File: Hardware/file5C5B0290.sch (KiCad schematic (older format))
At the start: 24 parts, among them J14 Eurorack Connector, U10 LM1117-5.0, U11 L7809, U9 LM1117-3.3

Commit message: Started board layout
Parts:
- added C46, C47: 22 uF, Capacitors_SMD:CP_Elec_4x5.3, symbol Device:CP
- added C48: 100 nF, Capacitors_SMD:C_0603, symbol Device:C
- added FB4: Ferrite_Bead, symbol Device:Ferrite_Bead
- added U13: LM1117-3.3, TO_SOT_Packages_SMD:SOT-223-3_TabPin2, symbol Regulator_Linear:LM1117-3.3
- C33, C34, C35, C36, C37, C38, C42, C43: footprint (none) -> Capacitors_SMD:CP_Elec_4x5.3
- C39, C40, C41, C44: footprint (none) -> Capacitors_SMD:C_0603
- U10, U9: footprint (none) -> TO_SOT_Packages_SMD:SOT-223-3_TabPin2
- U11: footprint (none) -> TO_SOT_Packages_SMD:TO-252-3_TabPin2
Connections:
- net +12V: now also FB4.2
- net +3V3: now also C47.1, C48.1, U13.2 (VO); no longer C36.1, C39.1, U9.2 (VO)
- net GND: now also C46.2, C47.2, C48.2, U13.1 (GND)
- new net: C46.1, FB4.1, U13.3 (VI)
- new net +3.3VA: C36.1, C39.1, U9.2 (VO)
- no-connect marks 0 -> 6
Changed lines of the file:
@@
 F 0 "U9" H 3450 2992 50  0000 C CNN
 F 1 "LM1117-3.3" H 3450 2901 50  0000 C CNN
-F 2 "" H 3450 2750 50  0001 C CNN
+F 2 "TO_SOT_Packages_SMD:SOT-223-3_TabPin2" H 3450 2750 50  0001 C CNN
 F 3 "http://www.ti.com/lit/ds/symlink/lm1117.pdf" H 3450 2750 50  0001 C CNN
 	1    3450 2750
@@
 L power:+12V #PWR0204
 U 1 1 5C5B0D76
-P 2500 2500
-F 0 "#PWR0204" H 2500 2350 50  0001 C CNN
-F 1 "+12V" H 2515 2673 50  0000 C CNN
-F 2 "" H 2500 2500 50  0001 C CNN
-F 3 "" H 2500 2500 50  0001 C CNN
-	1    2500 2500
+P 2500 1400
+F 0 "#PWR0204" H 2500 1250 50  0001 C CNN
+F 1 "+12V" H 2515 1573 50  0000 C CNN
+F 2 "" H 2500 1400 50  0001 C CNN
+F 3 "" H 2500 1400 50  0001 C CNN
+	1    2500 1400
 	1    0    0    -1
 $EndComp
@@
 F 0 "C39" H 4565 2996 50  0000 L CNN
 F 1 "100 nF" H 4565 2905 50  0000 L CNN
-F 2 "" H 4488 2800 50  0001 C CNN
+F 2 "Capacitors_SMD:C_0603" H 4488 2800 50  0001 C CNN
 F 3 "~" H 4450 2950 50  0001 C CNN
 	1    4450 2950
@@
 L power:+3.3V #PWR0206
 U 1 1 5C5B1292
-P 4450 2500
-F 0 "#PWR0206" H 4450 2350 50  0001 C CNN
-F 1 "+3.3V" H 4465 2673 50  0000 C CNN
-F 2 "" H 4450 2500 50  0001 C CNN
-F 3 "" H 4450 2500 50  0001 C CNN
-	1    4450 2500
-	1    0    0    -1
-$EndComp
-Wire Wire Line
-	4450 2500 4450 2750
-Connection ~ 4450 2750
+P 4450 1400
+F 0 "#PWR0206" H 4450 1250 50  0001 C CNN
+F 1 "+3.3V" H 4465 1573 50  0000 C CNN
+F 2 "" H 4450 1400 50  0001 C CNN
+F 3 "" H 4450 1400 50  0001 C CNN
+	1    4450 1400
+	1    0    0    -1
+$EndComp
 $Comp
 L Connector_Generic:Conn_02x08_Odd_Even J14
@@
 F 0 "C33" H 2968 2996 50  0000 L CNN
 F 1 "22 uF" H 2968 2905 50  0000 L CNN
-F 2 "" H 2888 2800 50  0001 C CNN
+F 2 "Capacitors_SMD:CP_Elec_4x5.3" H 2888 2800 50  0001 C CNN
 F 3 "~" H 2850 2950 50  0001 C CNN
 	1    2850 2950
@@
 F 0 "C36" H 4068 2996 50  0000 L CNN
 F 1 "22 uF" H 4068 2905 50  0000 L CNN
-F 2 "" H 3988 2800 50  0001 C CNN
+F 2 "Capacitors_SMD:CP_Elec_4x5.3" H 3988 2800 50  0001 C CNN
 F 3 "~" H 3950 2950 50  0001 C CNN
 	1    3950 2950
@@
 F 0 "C42" H 7668 3546 50  0000 L CNN
 F 1 "22 uF" H 7668 3455 50  0000 L CNN
-F 2 "" H 7588 3350 50  0001 C CNN
+F 2 "Capacitors_SMD:CP_Elec_4x5.3" H 7588 3350 50  0001 C CNN
 F 3 "~" H 7550 3500 50  0001 C CNN
 	1    7550 3500
@@
 F 0 "C43" H 7668 3996 50  0000 L CNN
 F 1 "22 uF" H 7668 3905 50  0000 L CNN
-F 2 "" H 7588 3800 50  0001 C CNN
+F 2 "Capacitors_SMD:CP_Elec_4x5.3" H 7588 3800 50  0001 C CNN
 F 3 "~" H 7550 3950 50  0001 C CNN
 	1    7550 3950
@@
 F 0 "C40" H 4565 3996 50  0000 L CNN
 F 1 "100 nF" H 4565 3905 50  0000 L CNN
-F 2 "" H 4488 3800 50  0001 C CNN
+F 2 "Capacitors_SMD:C_0603" H 4488 3800 50  0001 C CNN
 F 3 "~" H 4450 3950 50  0001 C CNN
 	1    4450 3950
@@
 F 0 "C34" H 2968 3996 50  0000 L CNN
 F 1 "22 uF" H 2968 3905 50  0000 L CNN
-F 2 "" H 2888 3800 50  0001 C CNN
+F 2 "Capacitors_SMD:CP_Elec_4x5.3" H 2888 3800 50  0001 C CNN
 F 3 "~" H 2850 3950 50  0001 C CNN
 	1    2850 3950
@@
 F 0 "C37" H 4068 3996 50  0000 L CNN
 F 1 "22 uF" H 4068 3905 50  0000 L CNN
-F 2 "" H 3988 3800 50  0001 C CNN
+F 2 "Capacitors_SMD:CP_Elec_4x5.3" H 3988 3800 50  0001 C CNN
 F 3 "~" H 3950 3950 50  0001 C CNN
 	1    3950 3950
@@
 F 0 "U10" H 3450 3992 50  0000 C CNN
 F 1 "LM1117-5.0" H 3450 3901 50  0000 C CNN
-F 2 "" H 3450 3750 50  0001 C CNN
+F 2 "TO_SOT_Packages_SMD:SOT-223-3_TabPin2" H 3450 3750 50  0001 C CNN
 F 3 "http://www.ti.com/lit/ds/symlink/lm1117.pdf" H 3450 3750 50  0001 C CNN
 	1    3450 3750
@@
 F 0 "C41" H 4565 4996 50  0000 L CNN
 F 1 "100 nF" H 4565 4905 50  0000 L CNN
-F 2 "" H 4488 4800 50  0001 C CNN
+F 2 "Capacitors_SMD:C_0603" H 4488 4800 50  0001 C CNN
 F 3 "~" H 4450 4950 50  0001 C CNN
 	1    4450 4950
@@
 F 0 "C35" H 2968 4996 50  0000 L CNN
 F 1 "22 uF" H 2968 4905 50  0000 L CNN
-F 2 "" H 2888 4800 50  0001 C CNN
+F 2 "Capacitors_SMD:CP_Elec_4x5.3" H 2888 4800 50  0001 C CNN
 F 3 "~" H 2850 4950 50  0001 C CNN
 	1    2850 4950
@@
 F 0 "C38" H 4068 4996 50  0000 L CNN
 F 1 "22 uF" H 4068 4905 50  0000 L CNN
-F 2 "" H 3988 4800 50  0001 C CNN
+F 2 "Capacitors_SMD:CP_Elec_4x5.3" H 3988 4800 50  0001 C CNN
 F 3 "~" H 3950 4950 50  0001 C CNN
 	1    3950 4950
@@
 F 0 "U11" H 3450 4992 50  0000 C CNN
 F 1 "L7809" H 3450 4901 50  0000 C CNN
-F 2 "" H 3475 4600 50  0001 L CIN
+F 2 "TO_SOT_Packages_SMD:TO-252-3_TabPin2" H 3475 4600 50  0001 L CIN
 F 3 "http://www.st.com/content/ccc/resource/technical/document/datasheet/41/4f/b3/b0/12/d4/47/88/CD00000444.pdf/files/CD00000444.pdf/jcr:content/translations/en.CD00000444.pdf" H 3450 4700 50  0001 C CNN
 	1    3450 4750
@@
 F 0 "C44" H 8965 3996 50  0000 L CNN
 F 1 "100 nF" H 8965 3905 50  0000 L CNN
-F 2 "" H 8888 3800 50  0001 C CNN
+F 2 "Capacitors_SMD:C_0603" H 8888 3800 50  0001 C CNN
 F 3 "~" H 8850 3950 50  0001 C CNN
 	1    8850 3950
@@
 	0    1    1    0
 $EndComp
-Wire Wire Line
-	2500 2500 2500 2750
 Connection ~ 2500 3750
 Wire Wire Line
@@
 	0    1    1    0
 $EndComp
+Wire Wire Line
+	2500 2750 2500 3750
+$Comp
+L Regulator_Linear:LM1117-3.3 U13
+U 1 1 5BDDA893
+P 3450 1750
+F 0 "U13" H 3450 1992 50  0000 C CNN
+F 1 "LM1117-3.3" H 3450 1901 50  0000 C CNN
+F 2 "TO_SOT_Packages_SMD:SOT-223-3_TabPin2" H 3450 1750 50  0001 C CNN
+F 3 "http://www.ti.com/lit/ds/symlink/lm1117.pdf" H 3450 1750 50  0001 C CNN
+	1    3450 1750
+	1    0    0    -1
+$EndComp
+Wire Wire Line
+	2850 1750 3150 1750
+$Comp
+L power:GND #PWR010
+U 1 1 5BDDA89B
+P 3450 2200
+F 0 "#PWR010" H 3450 1950 50  0001 C CNN
+F 1 "GND" H 3455 2027 50  0000 C CNN
+F 2 "" H 3450 2200 50  0001 C CNN
+F 3 "" H 3450 2200 50  0001 C CNN
+	1    3450 2200
+	1    0    0    -1
+$EndComp
+Wire Wire Line
+	3450 2200 3450 2150
+Wire Wire Line
+	2850 1800 2850 1750
+Wire Wire Line
+	2850 1750 2800 1750
+Connection ~ 2850 1750
+Wire Wire Line
+	2850 2100 2850 2150
+Wire Wire Line
+	2850 2150 3450 2150
+Connection ~ 3450 2150
+Wire Wire Line
+	3450 2150 3450 2050
+Wire Wire Line
+	3450 2150 3950 2150
+Wire Wire Line
+	3950 2150 3950 2100
+Wire Wire Line
+	3950 1800 3950 1750
+Wire Wire Line
+	3950 1750 3750 1750
+$Comp
+L Device:C C48
+U 1 1 5BDDA8AD
+P 4450 1950
+F 0 "C48" H 4565 1996 50  0000 L CNN
+F 1 "100 nF" H 4565 1905 50  0000 L CNN
+F 2 "Capacitors_SMD:C_0603" H 4488 1800 50  0001 C CNN
+F 3 "~" H 4450 1950 50  0001 C CNN
+	1    4450 1950
+	1    0    0    -1
+$EndComp
+Wire Wire Line
+	4450 2100 4450 2150
+Wire Wire Line
+	4450 2150 3950 2150
+Connection ~ 3950 2150
+Wire Wire Line
+	3950 1750 4450 1750
+Wire Wire Line
+	4450 1750 4450 1800
+Connection ~ 3950 1750
+$Comp
+L Device:CP C46
+U 1 1 5BDDA8BC
+P 2850 1950
+F 0 "C46" H 2968 1996 50  0000 L CNN
+F 1 "22 uF" H 2968 1905 50  0000 L CNN
+F 2 "Capacitors_SMD:CP_Elec_4x5.3" H 2888 1800 50  0001 C CNN
+F 3 "~" H 2850 1950 50  0001 C CNN
+	1    2850 1950
+	1    0    0    -1
+$EndComp
+$Comp
+L Device:CP C47
+U 1 1 5BDDA8C3
+P 3950 1950
+F 0 "C47" H 4068 1996 50  0000 L CNN
+F 1 "22 uF" H 4068 1905 50  0000 L CNN
+F 2 "Capacitors_SMD:CP_Elec_4x5.3" H 3988 1800 50  0001 C CNN
+F 3 "~" H 3950 1950 50  0001 C CNN
+	1    3950 1950
+	1    0    0    -1
+$EndComp
+$Comp
+L Device:Ferrite_Bead FB4
+U 1 1 5BDDA8CB
+P 2650 1750
+F 0 "FB4" V 2376 1750 50  0000 C CNN
+F 1 "Ferrite_Bead" V 2467 1750 50  0000 C CNN
+F 2 "" V 2580 1750 50  0001 C CNN
+F 3 "~" H 2650 1750 50  0001 C CNN
+	1    2650 1750
+	0    1    1    0
+$EndComp
+Connection ~ 2500 1750
+Connection ~ 4450 1750
+$Comp
+L power:+3.3VA #PWR011
+U 1 1 5BDE9E2A
+P 4450 2650
+F 0 "#PWR011" H 4450 2500 50  0001 C CNN
+F 1 "+3.3VA" H 4465 2823 50  0000 C CNN
+F 2 "" H 4450 2650 50  0001 C CNN
+F 3 "" H 4450 2650 50  0001 C CNN
+	1    4450 2650
+	1    0    0    -1
+$EndComp
+Wire Wire Line
+	4450 2650 4450 2750
+Connection ~ 4450 2750
+Wire Wire Line
+	2500 1400 2500 1750
+Wire Wire Line
+	4450 1400 4450 1750
+Wire Wire Line
+	2500 1750 2500 2750
 Connection ~ 2500 2750
-Wire Wire Line
-	2500 2750 2500 3750
+NoConn ~ 5750 3350
+NoConn ~ 5750 3450
+NoConn ~ 5750 3550
+NoConn ~ 6250 3350
+NoConn ~ 6250 3450
+NoConn ~ 6250 3550
 $EndSCHEMATC

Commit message: Fixed issues with footprints
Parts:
- C33, C34, C35, C36, C37, C38, C42, C43, C46, C47: footprint Capacitors_SMD:CP_Elec_4x5.3 -> Capacitor_SMD:CP_Elec_4x5.3
- C39, C40, C41, C44, C48: footprint Capacitors_SMD:C_0603 -> Capacitor_SMD:C_0603_1608Metric
- U10, U13, U9: footprint TO_SOT_Packages_SMD:SOT-223-3_TabPin2 -> Package_TO_SOT_SMD:SOT-223-3_TabPin2
- U11: footprint TO_SOT_Packages_SMD:TO-252-3_TabPin2 -> Package_TO_SOT_SMD:TO-252-3_TabPin2
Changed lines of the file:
@@
 F 0 "U9" H 3450 2992 50  0000 C CNN
 F 1 "LM1117-3.3" H 3450 2901 50  0000 C CNN
-F 2 "TO_SOT_Packages_SMD:SOT-223-3_TabPin2" H 3450 2750 50  0001 C CNN
+F 2 "Package_TO_SOT_SMD:SOT-223-3_TabPin2" H 3450 2750 50  0001 C CNN
 F 3 "http://www.ti.com/lit/ds/symlink/lm1117.pdf" H 3450 2750 50  0001 C CNN
 	1    3450 2750
@@
 F 0 "C39" H 4565 2996 50  0000 L CNN
 F 1 "100 nF" H 4565 2905 50  0000 L CNN
-F 2 "Capacitors_SMD:C_0603" H 4488 2800 50  0001 C CNN
+F 2 "Capacitor_SMD:C_0603_1608Metric" H 4488 2800 50  0001 C CNN
 F 3 "~" H 4450 2950 50  0001 C CNN
 	1    4450 2950
@@
 F 0 "C33" H 2968 2996 50  0000 L CNN
 F 1 "22 uF" H 2968 2905 50  0000 L CNN
-F 2 "Capacitors_SMD:CP_Elec_4x5.3" H 2888 2800 50  0001 C CNN
+F 2 "Capacitor_SMD:CP_Elec_4x5.3" H 2888 2800 50  0001 C CNN
 F 3 "~" H 2850 2950 50  0001 C CNN
 	1    2850 2950
@@
 F 0 "C36" H 4068 2996 50  0000 L CNN
 F 1 "22 uF" H 4068 2905 50  0000 L CNN
-F 2 "Capacitors_SMD:CP_Elec_4x5.3" H 3988 2800 50  0001 C CNN
+F 2 "Capacitor_SMD:CP_Elec_4x5.3" H 3988 2800 50  0001 C CNN
 F 3 "~" H 3950 2950 50  0001 C CNN
 	1    3950 2950
@@
 F 0 "C42" H 7668 3546 50  0000 L CNN
 F 1 "22 uF" H 7668 3455 50  0000 L CNN
-F 2 "Capacitors_SMD:CP_Elec_4x5.3" H 7588 3350 50  0001 C CNN
+F 2 "Capacitor_SMD:CP_Elec_4x5.3" H 7588 3350 50  0001 C CNN
 F 3 "~" H 7550 3500 50  0001 C CNN
 	1    7550 3500
@@
 F 0 "C43" H 7668 3996 50  0000 L CNN
 F 1 "22 uF" H 7668 3905 50  0000 L CNN
-F 2 "Capacitors_SMD:CP_Elec_4x5.3" H 7588 3800 50  0001 C CNN
+F 2 "Capacitor_SMD:CP_Elec_4x5.3" H 7588 3800 50  0001 C CNN
 F 3 "~" H 7550 3950 50  0001 C CNN
 	1    7550 3950
@@
 F 0 "C40" H 4565 3996 50  0000 L CNN
 F 1 "100 nF" H 4565 3905 50  0000 L CNN
-F 2 "Capacitors_SMD:C_0603" H 4488 3800 50  0001 C CNN
+F 2 "Capacitor_SMD:C_0603_1608Metric" H 4488 3800 50  0001 C CNN
 F 3 "~" H 4450 3950 50  0001 C CNN
 	1    4450 3950
@@
 F 0 "C34" H 2968 3996 50  0000 L CNN
 F 1 "22 uF" H 2968 3905 50  0000 L CNN
-F 2 "Capacitors_SMD:CP_Elec_4x5.3" H 2888 3800 50  0001 C CNN
+F 2 "Capacitor_SMD:CP_Elec_4x5.3" H 2888 3800 50  0001 C CNN
 F 3 "~" H 2850 3950 50  0001 C CNN
 	1    2850 3950
@@
 F 0 "C37" H 4068 3996 50  0000 L CNN
 F 1 "22 uF" H 4068 3905 50  0000 L CNN
-F 2 "Capacitors_SMD:CP_Elec_4x5.3" H 3988 3800 50  0001 C CNN
+F 2 "Capacitor_SMD:CP_Elec_4x5.3" H 3988 3800 50  0001 C CNN
 F 3 "~" H 3950 3950 50  0001 C CNN
 	1    3950 3950
@@
 F 0 "U10" H 3450 3992 50  0000 C CNN
 F 1 "LM1117-5.0" H 3450 3901 50  0000 C CNN
-F 2 "TO_SOT_Packages_SMD:SOT-223-3_TabPin2" H 3450 3750 50  0001 C CNN
+F 2 "Package_TO_SOT_SMD:SOT-223-3_TabPin2" H 3450 3750 50  0001 C CNN
 F 3 "http://www.ti.com/lit/ds/symlink/lm1117.pdf" H 3450 3750 50  0001 C CNN
 	1    3450 3750
@@
 F 0 "C41" H 4565 4996 50  0000 L CNN
 F 1 "100 nF" H 4565 4905 50  0000 L CNN
-F 2 "Capacitors_SMD:C_0603" H 4488 4800 50  0001 C CNN
+F 2 "Capacitor_SMD:C_0603_1608Metric" H 4488 4800 50  0001 C CNN
 F 3 "~" H 4450 4950 50  0001 C CNN
 	1    4450 4950
@@
 F 0 "C35" H 2968 4996 50  0000 L CNN
 F 1 "22 uF" H 2968 4905 50  0000 L CNN
-F 2 "Capacitors_SMD:CP_Elec_4x5.3" H 2888 4800 50  0001 C CNN
+F 2 "Capacitor_SMD:CP_Elec_4x5.3" H 2888 4800 50  0001 C CNN
 F 3 "~" H 2850 4950 50  0001 C CNN
 	1    2850 4950
@@
 F 0 "C38" H 4068 4996 50  0000 L CNN
 F 1 "22 uF" H 4068 4905 50  0000 L CNN
-F 2 "Capacitors_SMD:CP_Elec_4x5.3" H 3988 4800 50  0001 C CNN
+F 2 "Capacitor_SMD:CP_Elec_4x5.3" H 3988 4800 50  0001 C CNN
 F 3 "~" H 3950 4950 50  0001 C CNN
 	1    3950 4950
@@
 F 0 "U11" H 3450 4992 50  0000 C CNN
 F 1 "L7809" H 3450 4901 50  0000 C CNN
-F 2 "TO_SOT_Packages_SMD:TO-252-3_TabPin2" H 3475 4600 50  0001 L CIN
+F 2 "Package_TO_SOT_SMD:TO-252-3_TabPin2" H 3475 4600 50  0001 L CIN
 F 3 "http://www.st.com/content/ccc/resource/technical/document/datasheet/41/4f/b3/b0/12/d4/47/88/CD00000444.pdf/files/CD00000444.pdf/jcr:content/translations/en.CD00000444.pdf" H 3450 4700 50  0001 C CNN
 	1    3450 4750
@@
 F 0 "C44" H 8965 3996 50  0000 L CNN
 F 1 "100 nF" H 8965 3905 50  0000 L CNN
-F 2 "Capacitors_SMD:C_0603" H 8888 3800 50  0001 C CNN
+F 2 "Capacitor_SMD:C_0603_1608Metric" H 8888 3800 50  0001 C CNN
 F 3 "~" H 8850 3950 50  0001 C CNN
 	1    8850 3950
@@
 F 0 "U13" H 3450 1992 50  0000 C CNN
 F 1 "LM1117-3.3" H 3450 1901 50  0000 C CNN
-F 2 "TO_SOT_Packages_SMD:SOT-223-3_TabPin2" H 3450 1750 50  0001 C CNN
+F 2 "Package_TO_SOT_SMD:SOT-223-3_TabPin2" H 3450 1750 50  0001 C CNN
 F 3 "http://www.ti.com/lit/ds/symlink/lm1117.pdf" H 3450 1750 50  0001 C CNN
 	1    3450 1750
@@
 F 0 "C48" H 4565 1996 50  0000 L CNN
 F 1 "100 nF" H 4565 1905 50  0000 L CNN
-F 2 "Capacitors_SMD:C_0603" H 4488 1800 50  0001 C CNN
+F 2 "Capacitor_SMD:C_0603_1608Metric" H 4488 1800 50  0001 C CNN
 F 3 "~" H 4450 1950 50  0001 C CNN
 	1    4450 1950
@@
 F 0 "C46" H 2968 1996 50  0000 L CNN
 F 1 "22 uF" H 2968 1905 50  0000 L CNN
-F 2 "Capacitors_SMD:CP_Elec_4x5.3" H 2888 1800 50  0001 C CNN
+F 2 "Capacitor_SMD:CP_Elec_4x5.3" H 2888 1800 50  0001 C CNN
 F 3 "~" H 2850 1950 50  0001 C CNN
 	1    2850 1950
@@
 F 0 "C47" H 4068 1996 50  0000 L CNN
 F 1 "22 uF" H 4068 1905 50  0000 L CNN
-F 2 "Capacitors_SMD:CP_Elec_4x5.3" H 3988 1800 50  0001 C CNN
+F 2 "Capacitor_SMD:CP_Elec_4x5.3" H 3988 1800 50  0001 C CNN
 F 3 "~" H 3950 1950 50  0001 C CNN
 	1    3950 1950

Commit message: Added PJ398SM model
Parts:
- R50, R51: footprint (none) -> Resistor_SMD:R_0603_1608Metric
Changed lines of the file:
@@
 F 0 "R50" H 8520 3496 50  0000 L CNN
 F 1 "1k" H 8520 3405 50  0000 L CNN
-F 2 "" V 8380 3450 50  0001 C CNN
+F 2 "Resistor_SMD:R_0603_1608Metric" V 8380 3450 50  0001 C CNN
 F 3 "~" H 8450 3450 50  0001 C CNN
 	1    8450 3450
@@
 F 0 "R51" H 8920 3496 50  0000 L CNN
 F 1 "1k" H 8920 3405 50  0000 L CNN
-F 2 "" V 8780 3450 50  0001 C CNN
+F 2 "Resistor_SMD:R_0603_1608Metric" V 8780 3450 50  0001 C CNN
 F 3 "~" H 8850 3450 50  0001 C CNN
 	1    8850 3450

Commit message: Finished assigning footprints
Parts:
- D26, D27: value D -> 1N5819HW-7-F; footprint (none) -> Diode_SMD:D_SOD-123
- FB1, FB2, FB3, FB4: footprint (none) -> Inductor_SMD:L_0603_1608Metric
- J14: footprint (none) -> Connector_PinHeader_2.54mm:PinHeader_2x08_P2.54mm_Vertical
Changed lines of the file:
@@
 F 0 "J14" H 6100 3125 50  0000 C CNN
 F 1 "Eurorack Connector" H 6100 3216 50  0000 C CNN
-F 2 "" H 6050 3750 50  0001 C CNN
+F 2 "Connector_PinHeader_2.54mm:PinHeader_2x08_P2.54mm_Vertical" H 6050 3750 50  0001 C CNN
 F 3 "~" H 6050 3750 50  0001 C CNN
 	1    6050 3750
@@
 P 6000 4500
 F 0 "D27" V 5954 4579 50  0000 L CNN
-F 1 "D" V 6045 4579 50  0000 L CNN
-F 2 "" H 6000 4500 50  0001 C CNN
+F 1 "1N5819HW-7-F" V 6045 4579 50  0000 L CNN
+F 2 "Diode_SMD:D_SOD-123" H 6000 4500 50  0001 C CNN
 F 3 "~" H 6000 4500 50  0001 C CNN
 	1    6000 4500
@@
 P 6000 2800
 F 0 "D26" V 5954 2879 50  0000 L CNN
-F 1 "D" V 6045 2879 50  0000 L CNN
-F 2 "" H 6000 2800 50  0001 C CNN
+F 1 "1N5819HW-7-F" V 6045 2879 50  0000 L CNN
+F 2 "Diode_SMD:D_SOD-123" H 6000 2800 50  0001 C CNN
 F 3 "~" H 6000 2800 50  0001 C CNN
 	1    6000 2800
@@
 F 0 "FB2" V 2376 3750 50  0000 C CNN
 F 1 "Ferrite_Bead" V 2467 3750 50  0000 C CNN
-F 2 "" V 2580 3750 50  0001 C CNN
+F 2 "Inductor_SMD:L_0603_1608Metric" V 2580 3750 50  0001 C CNN
 F 3 "~" H 2650 3750 50  0001 C CNN
 	1    2650 3750
@@
 F 0 "FB3" V 2376 4750 50  0000 C CNN
 F 1 "Ferrite_Bead" V 2467 4750 50  0000 C CNN
-F 2 "" V 2580 4750 50  0001 C CNN
+F 2 "Inductor_SMD:L_0603_1608Metric" V 2580 4750 50  0001 C CNN
 F 3 "~" H 2650 4750 50  0001 C CNN
 	1    2650 4750
@@
 F 0 "FB1" V 2376 2750 50  0000 C CNN
 F 1 "Ferrite_Bead" V 2467 2750 50  0000 C CNN
-F 2 "" V 2580 2750 50  0001 C CNN
+F 2 "Inductor_SMD:L_0603_1608Metric" V 2580 2750 50  0001 C CNN
 F 3 "~" H 2650 2750 50  0001 C CNN
 	1    2650 2750
@@
 F 0 "FB4" V 2376 1750 50  0000 C CNN
 F 1 "Ferrite_Bead" V 2467 1750 50  0000 C CNN
-F 2 "" V 2580 1750 50  0001 C CNN
+F 2 "Inductor_SMD:L_0603_1608Metric" V 2580 1750 50  0001 C CNN
 F 3 "~" H 2650 1750 50  0001 C CNN
 	1    2650 1750

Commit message: Updated schematic
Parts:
- renumbered C46 to C39, C33 to C40, C34 to C41, C35 to C42, C47 to C43, C36 to C44, C37 to C45, C38 to C46, C48 to C47, C39 to C48, C40 to C49, C41 to C50, C42 to C51, C43 to C52, C44 to C53, D26 to D25, D27 to D26, D28 to D27, FB4 to FB1, FB1 to FB2, FB2 to FB3, FB3 to FB4, J14 to J15, R50 to R54, R51 to R55, U9 to U10, U10 to U11, U11 to U12, U13 to U9

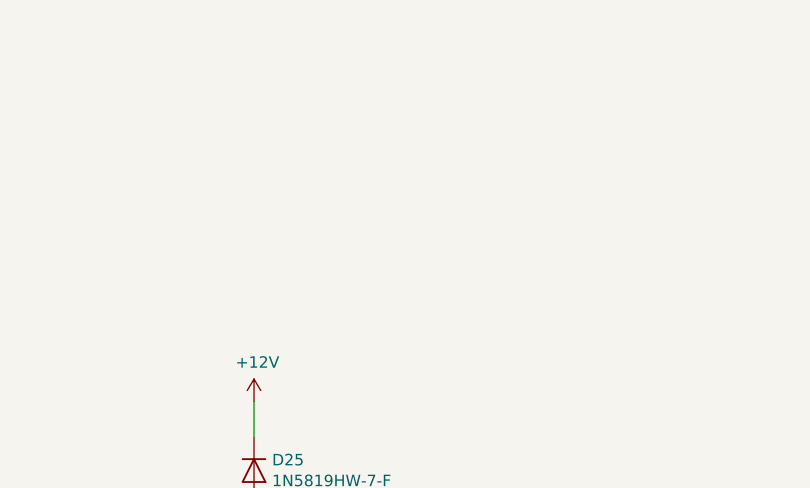
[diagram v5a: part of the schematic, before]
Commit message: Seperated two board with headers
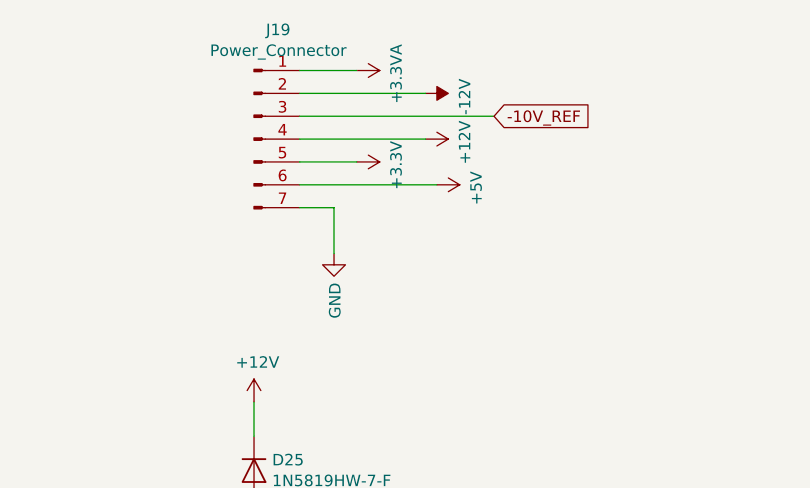
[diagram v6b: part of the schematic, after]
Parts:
- added J19: Power_Connector, Connector_PinHeader_2.54mm:PinHeader_1x07_P2.54mm_Vertical, symbol Connector:Conn_01x07_Male
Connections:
- net +12V: now also J19.4 (Pin_4)
- net +3.3VA: now also J19.1 (Pin_1)
- net +3V3: now also J19.5 (Pin_5)
- net +5V: now also J19.6 (Pin_6)
- net -10V_REF: now also J19.3 (Pin_3)
- net -12V: now also J19.2 (Pin_2)
- net GND: now also J19.7 (Pin_7)
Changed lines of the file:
@@
 NoConn ~ 6250 3450
 NoConn ~ 6250 3550
+$Comp
+L power:+3.3VA #PWR0151
+U 1 1 5BE74887
+P 6450 1050
+F 0 "#PWR0151" H 6450 900 50  0001 C CNN
+F 1 "+3.3VA" H 6465 1223 50  0000 C CNN
+F 2 "" H 6450 1050 50  0001 C CNN
+F 3 "" H 6450 1050 50  0001 C CNN
+	1    6450 1050
+	0    1    1    0
+$EndComp
+$Comp
+L power:+12V #PWR0157
+U 1 1 5BE748EC
+P 6750 1350
+F 0 "#PWR0157" H 6750 1200 50  0001 C CNN
+F 1 "+12V" H 6765 1523 50  0000 C CNN
+F 2 "" H 6750 1350 50  0001 C CNN
+F 3 "" H 6750 1350 50  0001 C CNN
+	1    6750 1350
+	0    1    1    0
+$EndComp
+$Comp
+L power:-12V #PWR0159
+U 1 1 5BE749C9
+P 6750 1150
+F 0 "#PWR0159" H 6750 1250 50  0001 C CNN
+F 1 "-12V" H 6765 1323 50  0000 C CNN
+F 2 "" H 6750 1150 50  0001 C CNN
+F 3 "" H 6750 1150 50  0001 C CNN
+	1    6750 1150
+	0    1    1    0
+$EndComp
+Wire Wire Line
+	6200 1050 6450 1050
+Wire Wire Line
+	6200 1150 6750 1150
+Wire Wire Line
+	6200 1350 6750 1350
+$Comp
+L power:GND #PWR0160
+U 1 1 5BE84728
+P 6350 1850
+F 0 "#PWR0160" H 6350 1600 50  0001 C CNN
+F 1 "GND" V 6355 1722 50  0000 R CNN
+F 2 "" H 6350 1850 50  0001 C CNN
+F 3 "" H 6350 1850 50  0001 C CNN
+	1    6350 1850
+	1    0    0    -1
+$EndComp
+Text GLabel 7050 1250 2    50   Input ~ 0
+-10V_REF
+Wire Wire Line
+	7050 1250 6200 1250
+$Comp
+L power:+3.3V #PWR0161
+U 1 1 5BE74822
+P 6450 1450
+F 0 "#PWR0161" H 6450 1300 50  0001 C CNN
+F 1 "+3.3V" H 6465 1623 50  0000 C CNN
+F 2 "" H 6450 1450 50  0001 C CNN
+F 3 "" H 6450 1450 50  0001 C CNN
+	1    6450 1450
+	0    1    1    0
+$EndComp
+Wire Wire Line
+	6200 1450 6450 1450
+$Comp
+L Connector:Conn_01x07_Male J19
+U 1 1 5C233DAA
+P 6000 1350
+F 0 "J19" H 6106 1828 50  0000 C CNN
+F 1 "Power_Connector" H 6106 1737 50  0000 C CNN
+F 2 "Connector_PinHeader_2.54mm:PinHeader_1x07_P2.54mm_Vertical" H 6000 1350 50  0001 C CNN
+F 3 "~" H 6000 1350 50  0001 C CNN
+	1    6000 1350
+	1    0    0    -1
+$EndComp
+Wire Wire Line
+	6350 1850 6350 1650
+Wire Wire Line
+	6350 1650 6200 1650
+$Comp
+L power:+5V #PWR0162
+U 1 1 5C23C2BC
+P 6800 1550
+F 0 "#PWR0162" H 6800 1400 50  0001 C CNN
+F 1 "+5V" H 6815 1723 50  0000 C CNN
+F 2 "" H 6800 1550 50  0001 C CNN
+F 3 "" H 6800 1550 50  0001 C CNN
+	1    6800 1550
+	0    1    1    0
+$EndComp
+Wire Wire Line
+	6800 1550 6200 1550
 $EndSCHEMATC
